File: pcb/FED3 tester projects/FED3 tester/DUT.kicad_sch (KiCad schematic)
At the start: 73 parts, among them J2 6pin_hd, J3 Conn_02x03_Odd_Even, J4 MotorCkeck, J5 Motor, J7 Conn_01x02_Socket, K1 1462042-8, K2 1462042-8, K3 1462042-8, Q1 DMN63D8L-7, Q3 DMN63D8L-7, Q4 DMN63D8L-7, U4 THS4281, U5 THS4281, U6 THS4281, U7 THS4281, U8 ZXCT1082

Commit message: FED3 Tester - 1º routing finalizado
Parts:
- C14, C15, C16, C17, C18, C19, C20, C21, C22, C23, C24, C25: footprint Capacitor_SMD:C_0402_1005Metric_Pad0.74x0.62mm_HandSolder -> Capacitor_SMD:C_0402_1005Metric
- K1, K2, K3: Check_prices https://www.snapeda.com/parts/1462042-8/TE+Connectivity+Pot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 -> (none); Description_1 Signal Relay 5VDC 2A SPDT (( 10mm 7.5mm 5.65mm)) Surface Mo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 -> (none); EU_RoHS_Compliance Compliant -> (none); MANUFACTURER TE Connectivity -> (none); MF TE Connectivity -> (none); MP 1462042-8 -> (none); PARTREV 0917 -> (none); Package None -> (none); Price None -> (none); STANDARD Manufacturer recommendation -> (none); SnapEDA_Link https://www.snapeda.com/parts/1462042-8/TE+Connectivity+Pot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 -> (none)
- R26, R27: footprint Resistor_SMD:R_0603_1608Metric -> Resistor_SMD:R_0402_1005Metric
- TP10, TP11, TP12, TP13, TP2, TP3, TP4, TP5, TP6, TP7, TP8, TP9: footprint FED3_PCBLib:Pin_D1.75mm_1 -> FED3_PCBLib:Pin_D1.75mm
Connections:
- net USB+5V: no longer D1.1 (K), D10.1 (K), D8.1 (K), K1.8, K2.8, K3.8
- new net RELAY+5V: D1.1 (K), D10.1 (K), D8.1 (K), K1.8, K2.8, K3.8
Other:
- moved on the sheet: J7, R45

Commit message: FED3-tester
- 'final' - antes de revisão com o Filipe
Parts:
- C14, C15, C20, C21: MPN C1005X7R1E104K050BB -> CGA2B3X7R1H104K050BB; OEPSPN OEPS010050 -> OEPS010016; TYPE (none) -> SMD
- C16, C17, C18, C19, C22, C23, C24, C25, D1, D10, D8, Q1, Q3, Q4, R10, R11, R12, R13, R14, R15, R16, R17, R18, R19, R20, R21, R22, R23, R24, R9, U4, U5, U6, U7, U8: TYPE (none) -> SMD
- J2: MPN 67996-206HLF -> n.a; OEPSPN OEPS070015 -> n.a; TYPE TH -> n.a; now left out of the parts list
- J3: OEPSPN OEPS070124 -> TBD; TYPE (none) -> TH
- J4: value MotorCkeck -> MotorCkeck1; TYPE (none) -> TH
- J5: value Motor -> MotorCkeck2; TYPE (none) -> TH
- J7: MPN (none) -> TBD; OEPSPN (none) -> TBD; TYPE (none) -> TH
- K1, K2, K3: value 1462042-8 -> Relay SPDT; Comment 1462042-8 -> (none); MPN (none) -> 1462042-8; OEPSPN (none) -> TBD; TYPE (none) -> SMD
- R25: MPN xx -> ERJ-PA2J100X; OEPSPN xx -> OEPS020041; TYPE (none) -> SMD
- R26: MPN sdff -> TBD; OEPSPN qwefds -> TBD; TYPE (none) -> SMD
- R27: MPN aerg -> TBD; OEPSPN gedg -> TBD; TYPE (none) -> SMD
- R28, R43, R47: MPN ?? -> RCS0402100RFKED; OEPSPN ?? -> OEPS020028; TYPE (none) -> SMD
- R29, R44, R48: OEPSPN CPF0402B10KE1 -> OEPS020043; TYPE (none) -> SMD
- R30, R46: MPN sth -> TBD; OEPSPN srths -> TBD; TYPE (none) -> SMD
- R45: MPN b6ryh -> TBD; OEPSPN 456yert -> TBD; TYPE (none) -> SMD
- R49, R50: MPN xxx -> CRCW04021K00FKED; OEPSPN ??? -> OEPS020027; TYPE (none) -> SMD
- TP10, TP11, TP12, TP13, TP2, TP3, TP4, TP5, TP6, TP7, TP8, TP9: MPN (none) -> n.a; OEPSPN (none) -> n.a; TYPE (none) -> n.a
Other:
- moved on the sheet: D8, J7, K2, Q3, R43, R44, R49, R50, TP10, TP11, TP12, TP13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

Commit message: FED 3 tester - actualizados novos OEPSPN & MPN; ainda 1 em falta
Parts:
- J3: MPN PR20203VBDN -> 61300511021
- J4: MPN TBD -> PPTC051LFBN-RC; OEPSPN TBD -> OEPS070142
- J5: MPN TBD -> 61300511021; OEPSPN TBD -> OEPS070143
- J7: MPN TBD -> PPTC021LFBN-RC; OEPSPN TBD -> OEPS070095
- K1, K2, K3: OEPSPN TBD -> OEPS100078
- R26, R27: MPN TBD -> ERA-2AEB122X; OEPSPN TBD -> OEPS020213
- R30: MPN TBD -> ERA-2AEB223X; OEPSPN TBD -> OEPS020212
- R45: MPN TBD -> CRCW040210M0FKED; OEPSPN TBD -> OEPS020211
- R46: MPN TBD -> CRCW04022M00FKEDC; OEPSPN TBD -> OEPS020210
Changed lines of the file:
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@@
 			)
 		)
-		(property "MPN" "TBD"
+		(property "MPN" "CRCW040210M0FKED"
 			(at 107.823 138.938 0)
 			(effects
@@
 			)
 		)
-		(property "OEPSPN" "TBD"
+		(property "OEPSPN" "OEPS020211"
 			(at 99.06 135.89 0)
 			(effects
@@
 			)
 		)
-		(property "Description" "Generic connector, single row, 01x05"
+		(property "Description" "CONN RCPT 2.54mm 5POS"
 			(at 265.43 66.04 0)
 			(effects
@@
 			)
 		)
-		(property "OEPSPN" "TBD"
+		(property "OEPSPN" "OEPS070142"
 			(at 265.43 66.04 0)
 			(effects
@@
 			)
 		)
-		(property "MPN" "TBD"
+		(property "MPN" "PPTC051LFBN-RC"
 			(at 265.43 66.04 0)
 			(effects
@@
 			)
 		)
-		(property "MPN" "TBD"
+		(property "MPN" "ERA-2AEB122X"
 			(at 114.427 141.478 0)
 			(effects
@@
 			)
 		)
-		(property "OEPSPN" "TBD"
+		(property "OEPSPN" "OEPS020213"
 			(at 123.19 138.43 0)
 			(effects
@@
 			)
 		)
-		(property "Description" "Generic connector, single row, 01x05"
+		(property "Description" "CONN HEADER R/A 5POS 2.54MM"
 			(at 265.43 83.82 0)
 			(effects
@@
 			)
 		)
-		(property "OEPSPN" "TBD"
+		(property "OEPSPN" "OEPS070143"
 			(at 265.43 83.82 0)
 			(effects
@@
 			)
 		)
-		(property "MPN" "TBD"
+		(property "MPN" "61300511021"
 			(at 265.43 83.82 0)
 			(effects
@@
 			)
 		)
-		(property "MPN" "TBD"
+		(property "MPN" "ERA-2AEB223X"
 			(at 97.917 175.768 0)
 			(effects
@@
 			)
 		)
-		(property "OEPSPN" "TBD"
+		(property "OEPSPN" "OEPS020212"
 			(at 106.68 172.72 0)
 			(effects
@@
 			)
 		)
-		(property "MPN" "TBD"
+		(property "MPN" "ERA-2AEB122X"
 			(at 109.347 141.478 0)
 			(effects
@@
 			)
 		)
-		(property "OEPSPN" "TBD"
+		(property "OEPSPN" "OEPS020213"
 			(at 118.11 138.43 0)
 			(effects
@@
 			)
 		)
-		(property "OEPSPN" "TBD"
+		(property "OEPSPN" "OEPS100078"
 			(at 82.55 162.56 0)
 			(effects
@@
 			)
 		)
-		(property "Description" "HEADER 2.54MM 90º 2x3POS"
+		(property "Description" ""
 			(at 262.89 41.91 0)
 			(effects
@@
 			)
 		)
-		(property "MPN" "PR20203VBDN"
+		(property "MPN" "61300511021"
 			(at 258.318 48.006 0)
 			(effects
@@
 			)
 		)
-		(property "Description" "Generic connector, single row, 01x02"
+		(property "Description" "HEADER RCPT 2.54MM straight 1x2POS"
 			(at 212.09 111.76 0)
 			(effects
@@
 			)
 		)
-		(property "OEPSPN" "TBD"
+		(property "OEPSPN" "OEPS070095"
 			(at 212.09 111.76 90)
 			(effects
@@
 			)
 		)
-		(property "MPN" "TBD"
+		(property "MPN" "PPTC021LFBN-RC"
 			(at 212.09 111.76 90)
 			(effects
@@
 			)
 		)
-		(property "MPN" "TBD"
+		(property "MPN" "CRCW04022M00FKEDC"
 			(at 131.953 165.862 0)
 			(effects
@@
 			)
 		)
-		(property "OEPSPN" "TBD"
+		(property "OEPSPN" "OEPS020210"
 			(at 123.19 168.91 0)
 			(effects
@@
 			)
 		)
-		(property "OEPSPN" "TBD"
+		(property "OEPSPN" "OEPS100078"
 			(at 62.23 129.54 0)
 			(effects
@@
 			)
 		)
-		(property "OEPSPN" "TBD"
+		(property "OEPSPN" "OEPS100078"
 			(at 199.39 130.81 0)
 			(effects

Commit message: final tunning??
- fields de componentes actualizados
- trocada polaridade na ficha botão de emergência
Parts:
- K1, K2, K3: Availability In Stock -> (none)
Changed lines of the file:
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@@
 			)
 		)
-		(property "Comment" ""
-			(at 82.55 162.56 0)
-			(effects
-				(font
-					(size 1.27 1.27)
-				)
-				(justify bottom)
-				(hide yes)
-			)
-		)
-		(property "Availability" "In Stock"
-			(at 82.55 162.56 0)
-			(effects
-				(font
-					(size 1.27 1.27)
-				)
-				(justify bottom)
-				(hide yes)
-			)
-		)
 		(property "OEPSPN" "OEPS100078"
 			(at 82.55 162.56 0)
@@
 			)
 		)
-		(property "Comment" ""
-			(at 62.23 129.54 0)
-			(effects
-				(font
-					(size 1.27 1.27)
-				)
-				(justify bottom)
-				(hide yes)
-			)
-		)
-		(property "Availability" "In Stock"
-			(at 62.23 129.54 0)
-			(effects
-				(font
-					(size 1.27 1.27)
-				)
-				(justify bottom)
-				(hide yes)
-			)
-		)
 		(property "OEPSPN" "OEPS100078"
 			(at 62.23 129.54 0)
@@
 				(hide yes)
 			)
-		)
-		(property "Comment" ""
-			(at 199.39 130.81 0)
-			(effects
-				(font
-					(size 1.27 1.27)
-				)
-				(justify bottom)
-				(hide yes)
-			)
-		)
-		(property "Availability" "In Stock"
-			(at 199.39 130.81 0)
-			(effects
-				(font
-					(size 1.27 1.27)
-				)
-				(justify bottom)
-				(hide yes)
-			)

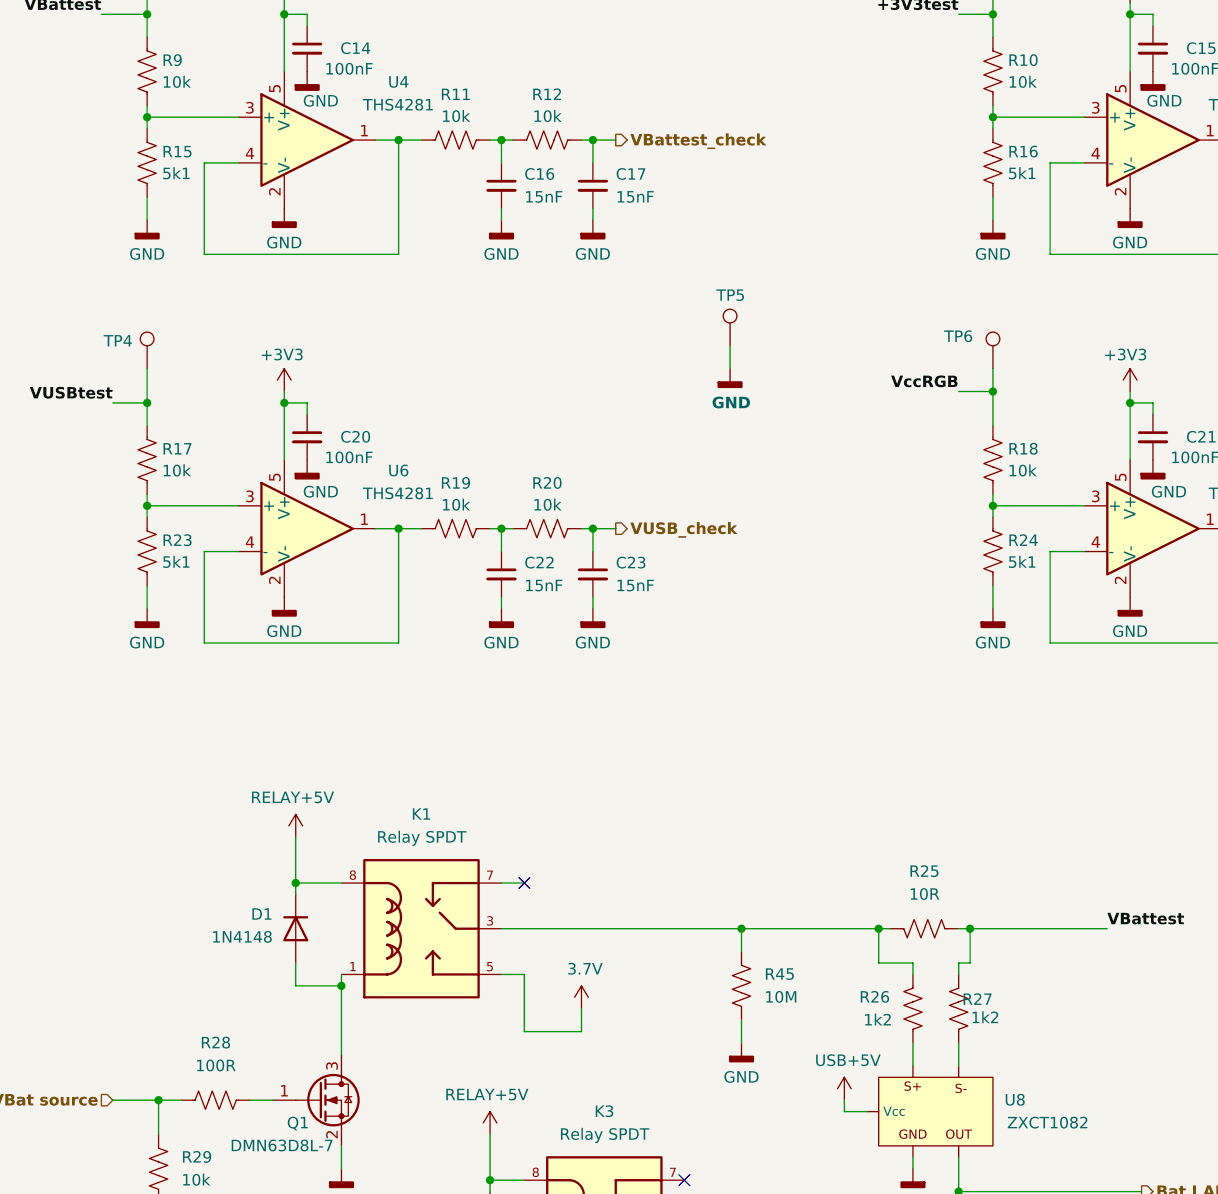
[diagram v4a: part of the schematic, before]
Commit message: tunning com v.7.7
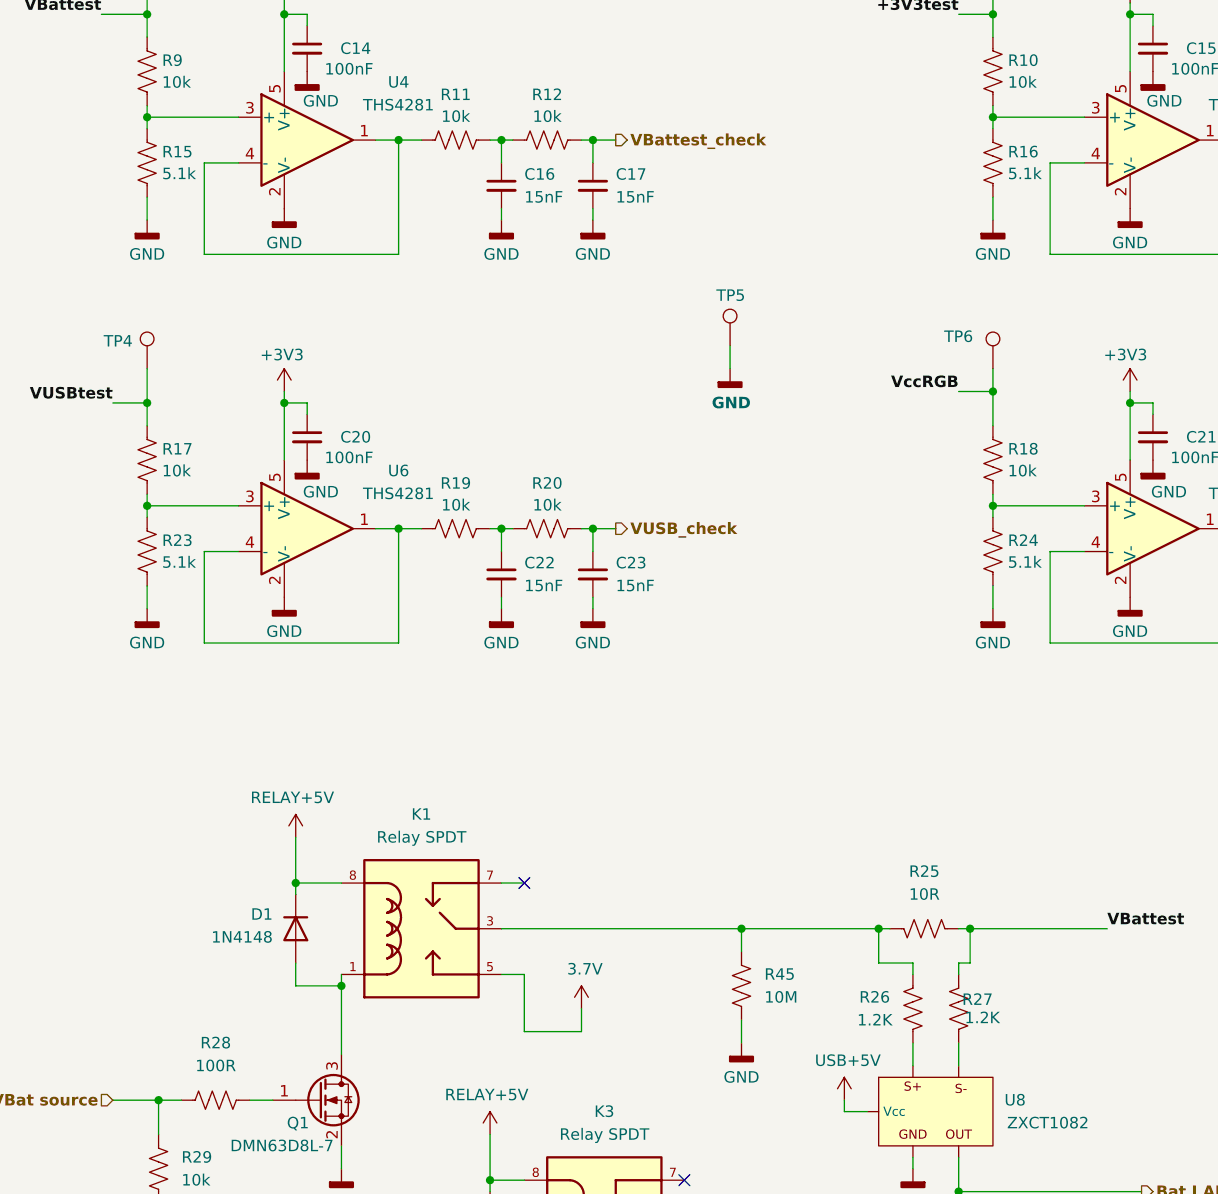
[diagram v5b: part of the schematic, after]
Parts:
- C14, C15, C20, C21: TYPE SMD -> (none); TempCo (none) -> X7R; Tolerance (none) -> 10%; Voltage (none) -> 50V
- C16, C17, C18, C19, C22, C23, C24, C25: TYPE SMD -> (none); TempCo (none) -> X7R; Tolerance (none) -> 10%; Voltage (none) -> 35V
- D1, D10, D8, K1, K2, K3, Q1, Q3, Q4, U4, U5, U6, U7, U8: TYPE SMD -> (none)
- J2, TP10, TP11, TP12, TP13, TP2, TP3, TP4, TP5, TP6, TP7, TP8, TP9: TYPE n.a -> (none)
- J3: OEPSPN TBD -> OEPS070143; TYPE TH -> (none)
- J4, J5, J7: TYPE TH -> (none)
- R10, R11, R12, R13, R14, R17, R18, R19, R20, R21, R22, R29, R30, R44, R48, R9: TYPE SMD -> (none); Tolerance (none) -> 0.1%
- R15, R16, R23, R24: value 5k1 -> 5.1k; TYPE SMD -> (none); Tolerance (none) -> 1%
- R25: TYPE SMD -> (none); Tolerance (none) -> 5%
- R26, R27: value 1k2 -> 1.2K; TYPE SMD -> (none); Tolerance (none) -> 0.1%
- R28, R43, R45, R46, R47, R49, R50: TYPE SMD -> (none); Tolerance (none) -> 1%
